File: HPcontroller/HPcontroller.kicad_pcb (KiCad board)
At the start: 4 copper layers, 100 x 39.8 mm, 64 parts, among them J1 Conn_01x02_Pin, J2 UJ20-C-H-G-SMT-1-P16-TR, J5 54-00174, SW1 SW_SPST, U1 PSSI2021SAY, U2 MCP3021A1T-E/OT, U4 NCP81071B, U5 AP33771C, U6 LM2904, U7 Adafruit_QTPY_ESP32-C3

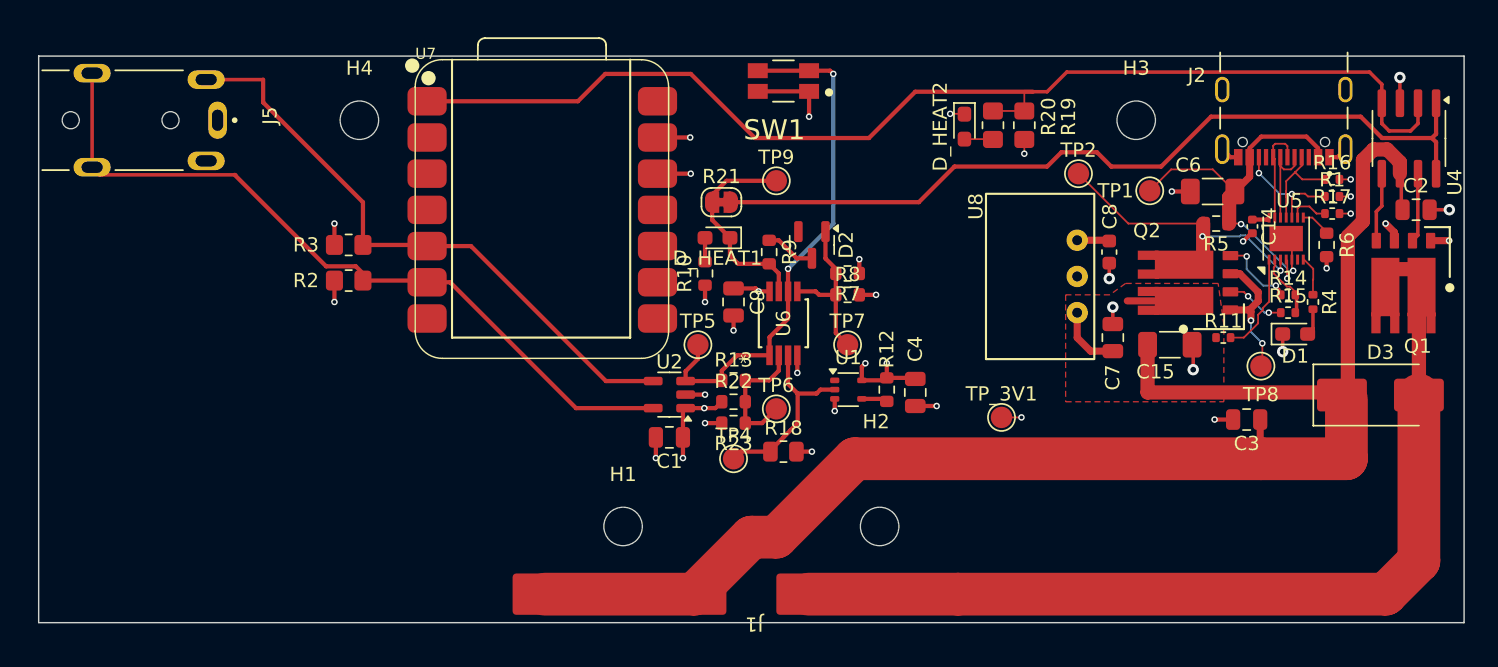
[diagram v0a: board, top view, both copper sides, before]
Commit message: released rev c - op amp swap not fixed!
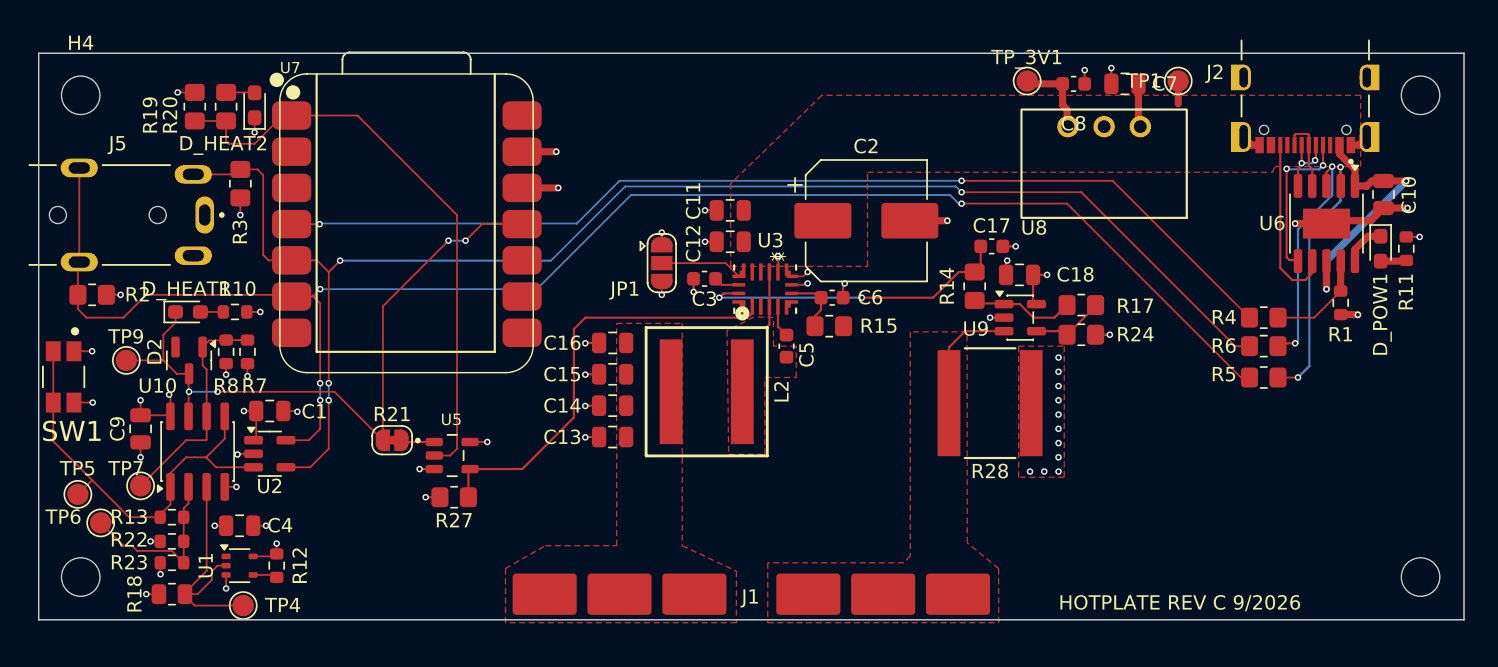
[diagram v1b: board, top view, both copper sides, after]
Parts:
- removed D1: LED, LED_SMD:LED_0603_1608Metric_Pad1.05x0.95mm_HandSolder
- removed D3: D, Diode_SMD:D_SMB_Handsoldering
- removed Q1, Q2: ~, hotplate_Library:LFPAK56D
- removed R16: 5k1 1%, Resistor_SMD:R_0402_1005Metric
- removed R9: 0, Resistor_SMD:R_0603_1608Metric
- removed TP2, TP8: TestPoint, TestPoint:TestPoint_Pad_D1.5mm
- removed U4: NCP81071B, Package_SO:SOIC-8_3.9x4.9mm_P1.27mm
- added C10: 10uF, Capacitor_SMD:C_0805_2012Metric, F.Cu at (179.6, 128.0)
- added C11: 10uF, Capacitor_SMD:C_0805_2012Metric, F.Cu at (133.8, 129.1)
- added C12: 10uF, Capacitor_SMD:C_0805_2012Metric, F.Cu at (133.8, 131.3)
- added C13: 10uF, Capacitor_SMD:C_0805_2012Metric, F.Cu at (125.5, 145.0)
- added C16: 10uF, Capacitor_SMD:C_0805_2012Metric, F.Cu at (125.5, 138.4)
- added C17: C, Capacitor_SMD:C_0603_1608Metric, F.Cu at (152.1, 131.6)
- added C18: 1uF, Capacitor_SMD:C_0805_2012Metric, F.Cu at (154.1, 133.6)
- added C5: 220n, Capacitor_SMD:C_0603_1608Metric, F.Cu at (137.7, 138.6)
- added D_POW1: LED, LED_SMD:LED_0603_1608Metric_Pad1.05x0.95mm_HandSolder, F.Cu at (179.4, 131.8)
- added JP1: Jumper_3_Open, Jumper:SolderJumper-3_P1.3mm_Open_RoundedPad1.0x1.5mm, F.Cu at (129.0, 132.8)
- added L2: 22u, HPcontroller_kimera:WE-XHMI_8080, F.Cu at (132.1, 141.8)
- added R24: 1.37k, Resistor_SMD:R_0805_2012Metric_Pad1.20x1.40mm_HandSolder, F.Cu at (158.4, 137.8)
- added R27: 10k, Resistor_SMD:R_0805_2012Metric_Pad1.20x1.40mm_HandSolder, F.Cu at (114.4, 149.2)
- added R28: 30m, HPcontroller_kimera:STA_CSSH2728_STP, F.Cu at (152.0, 142.6)
- added U10: MCP6002-xMS, Package_SO:SOIC-8_3.9x4.9mm_P1.27mm, F.Cu at (96.4, 146.0)
- added U3: MP4423CGLE-P, HPcontroller_kimera:QFN-16_MPQ4423C_MNP, F.Cu at (136.2, 134.6)
- added U9: MCP6001-OT, Package_TO_SOT_SMD:SOT-23-5, F.Cu at (154.1, 136.6)
- C14: value 1uF 25V -> 10uF; footprint Capacitor_SMD:C_0402_1005Metric -> Capacitor_SMD:C_0805_2012Metric
- C15: value 10uF 50V -> 10uF; footprint Capacitor_SMD:C_1206_3216Metric_Pad1.33x1.80mm_HandSolder -> Capacitor_SMD:C_0805_2012Metric
- C2: value 1uF -> 100u; footprint Capacitor_SMD:C_0805_2012Metric -> Capacitor_SMD:CP_Elec_8x6.7
- C3: value 10u -> 1u; footprint Capacitor_SMD:C_0805_2012Metric -> Capacitor_SMD:C_0603_1608Metric
- C6: value 10uF 50V -> 220n; footprint Capacitor_SMD:C_1206_3216Metric_Pad1.33x1.80mm_HandSolder -> Capacitor_SMD:C_0603_1608Metric
- R1: value 5k1 1% -> 210k; footprint Resistor_SMD:R_0402_1005Metric -> Resistor_SMD:R_0603_1608Metric
- R11: footprint Resistor_SMD:R_0402_1005Metric -> Resistor_SMD:R_0603_1608Metric
- R14: value 10 -> 0; footprint Resistor_SMD:R_0402_1005Metric -> Resistor_SMD:R_0805_2012Metric_Pad1.20x1.40mm_HandSolder
- R15: footprint Resistor_SMD:R_0402_1005Metric -> Resistor_SMD:R_0805_2012Metric_Pad1.20x1.40mm_HandSolder
- R17: value 5k1 1% -> 5.9k; footprint Resistor_SMD:R_0402_1005Metric -> Resistor_SMD:R_0805_2012Metric_Pad1.20x1.40mm_HandSolder
- R4: value 1k -> 0; footprint Resistor_SMD:R_0402_1005Metric -> Resistor_SMD:R_0805_2012Metric_Pad1.20x1.40mm_HandSolder
- R5: value 5m -> 0; footprint Resistor_SMD:R_0603_1608Metric -> Resistor_SMD:R_0805_2012Metric_Pad1.20x1.40mm_HandSolder
- R6: value 26k -> 0; footprint Resistor_SMD:R_0603_1608Metric -> Resistor_SMD:R_0805_2012Metric_Pad1.20x1.40mm_HandSolder
- U5: value AP33771C -> SN74LVC1G08DBVR; footprint Package_DFN_QFN:DFN-14-1EP_3x3mm_P0.4mm_EP1.78x2.35mm -> HPcontroller_kimera:SOT95P280X145-5N
- U6: value LM2904 -> ~; footprint hotplate_Library:MINISO8_3P1X3P2X0P65_STM -> Package_SO:SSOP-10-1EP_3.9x4.9mm_P1mm_EP2.1x3.3mm
- moved U5 60.5 mm to (114.3, 146.3), turned to 0 degrees
- moved R19 58.2 mm to (96.2, 121.8), turned to 90 degrees
- moved H2 56.2 mm to (88.2, 154.8)
- moved H1 56.1 mm to (182.2, 154.8)
- moved SW1 54.6 mm to (87.0, 140.8), turned to -90 degrees
- moved R20 53.8 mm to (98.4, 121.8), turned to 90 degrees
- moved TP7 50.6 mm to (92.4, 148.4)
- moved D_HEAT2 49.8 mm to (100.4, 121.7), turned to 90 degrees
- moved C4 48.3 mm to (99.3, 151.2), turned to 180 degrees
- moved TP6 48.1 mm to (89.6, 151.0)
- moved TP9 47.3 mm to (91.4, 139.6)
- moved C14 46.6 mm to (125.5, 142.8), turned to 180 degrees
- moved TP5 44.7 mm to (88.0, 149.0)
- moved R12 44.5 mm to (102.0, 154.0)
- moved U1 44.5 mm to (99.3, 154.0)
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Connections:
- C14 pad 1: Net-(U5-V5V) -> Net-(J1-Pin_1)
- C15 pad 1: +28V -> Net-(J1-Pin_1)
- C3 pad 1: +28V -> Net-(U3-VCC)
- C6 pad 1: /USB POWER IN/VUSB_RAW -> GND
- C6 pad 2: GND -> Net-(U3-OUT)
- D2 pad 3: Net-(D2-K) -> /HEATER DRIVE/ENABLE_HEATER_DRIVE
- J1 pad 1: +28V -> Net-(J1-Pin_1)
- J2 pad A4_B9: /USB POWER IN/VUSB_RAW -> +28V
- J2 pad B4_A9: /USB POWER IN/VUSB_RAW -> +28V
- R1 pad 1: /USB POWER IN/CC2 -> GND
- R1 pad 2: GND -> Net-(U6-CFG1)
- R11 pad 1: +28V -> +3V3
- R11 pad 2: Net-(U5-Vout) -> Net-(D_POW1-A)
- R13 pad 2: Net-(U6A--) -> Net-(U10A--)
- R14 pad 1: Net-(Q2-G2) -> /HEATER DRIVE/FB
- R14 pad 2: Net-(U5-PWR_EN) -> Net-(R14-Pad2)
- R15 pad 1: Net-(Q2-G1) -> Net-(U3-OUT)
- R15 pad 2: Net-(U5-PWR_EN) -> Net-(J1-Pin_1)
- R17 pad 1: Net-(U5-ISel) -> Net-(R14-Pad2)
- R17 pad 2: GND -> Net-(U9--)
- R18 pad 1: Net-(U6A-+) -> Net-(U10A-+)
- R21 pad 2: Net-(U4-ENA) -> Net-(U5-A)
- R22 pad 2: Net-(U6A--) -> Net-(U10A--)
- R23 pad 1: Net-(U6A--) -> Net-(U10A--)
- R4 pad 1: Net-(U5-LED) -> Net-(U6-CFG1)
- R4 pad 2: Net-(D1-A) -> /USB POWER IN/CFG1
- R5 pad 1: /USB POWER IN/VUSB_RAW -> /USB POWER IN/CFG2/SCL
- R5 pad 2: Net-(Q2-D2) -> /SCL
- R6 pad 1: Net-(U5-VSel) -> /USB POWER IN/CFG3/SDA
- R6 pad 2: GND -> /SDA
- TP1 pad 1: /USB POWER IN/VUSB_RAW -> +28V
- TP4 pad 1: Net-(U6A-+) -> Net-(U10A-+)
- TP6 pad 1: Net-(U6A--) -> Net-(U10A--)
- U1 pad 2: Net-(U6A-+) -> Net-(U10A-+)
- U5 pad 1: Net-(U5-Vout) -> Net-(U5-A)
- U5 pad 2: Net-(U5-PWR_EN) -> /HEAT_DRIVE
- U5 pad 3: Net-(Q2-D2) -> GND
- U5 pad 4: /USB POWER IN/VUSB_RAW -> /HEATER DRIVE/EN
- U5 pad 5: GND -> +3V3
- U6 pad 1: Net-(SW1-B) -> +28V
- U6 pad 2: Net-(U6A--) -> /USB POWER IN/CFG2/SCL
- U6 pad 3: Net-(U6A-+) -> /USB POWER IN/CFG3/SDA
- U6 pad 4: GND -> /USB POWER IN/DP
- U6 pad 5: Net-(D2-A) -> /USB POWER IN/DN
- U6 pad 6: Net-(SW1-B) -> /USB POWER IN/CC1
- U6 pad 7: /HEATER DRIVE/ENABLE_HEATER_DRIVE -> /USB POWER IN/CC2
- U6 pad 8: +3V3 -> +28V
- U7 pad 11: unconnected-(U7-MOSI-Pad11) -> /HEATER DRIVE/ENABLE_HEATER_DRIVE
- U7 pad 4: unconnected-(U7-A3-Pad4) -> /USB POWER IN/CFG1
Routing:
- net +28V: track 117.6 -> 23.4 mm, vias 0 -> 2
- net /USB POWER IN/CFG1: track 0.00 -> 72.4 mm, vias 0 -> 2
- net /SDA: track 42.8 -> 103.6 mm, vias 0 -> 4
- net /SCL: track 53.3 -> 113.6 mm, vias 0 -> 4
- net Net-(J1-Pin_2): track 66.9 -> 8.25 mm
- net Net-(U4-ENA): track 58.3 -> 0.00 mm
- net /HEAT_DRIVE: track 83.2 -> 41.8 mm
- net /HEATER DRIVE/ENABLE_HEATER_DRIVE: track 14.9 -> 48.1 mm, vias 0 -> 4
- net /HEATER DRIVE/EN: track 0.00 -> 30.5 mm
- net /USB POWER IN/VUSB_RAW: track 26.7 -> 0.00 mm, vias 2 -> 0
- net /HEATER DRIVE/FB: track 0.00 -> 22.3 mm, vias 0 -> 2
- net Net-(Q2-D2): track 20.4 -> 0.00 mm, vias 2 -> 0
- net /USB POWER IN/CFG2/SCL: track 0.00 -> 18.7 mm, vias 0 -> 2
- net Net-(U10A-+): track 0.00 -> 16.7 mm
- net /USB POWER IN/CFG3/SDA: track 0.00 -> 16.4 mm, vias 0 -> 2
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- added copper zone on In2.Cu, net +3V3
- added copper zone on F.Cu, net GND
- added copper zone on In1.Cu, net GND
- added copper zone on F.Cu, net Net-(C5-Pad2)
- added copper zone on F.Cu, net Net-(J1-Pin_1)
- added copper zone on F.Cu, net Net-(J1-Pin_2)
- removed copper zone on In1.Cu, net +3V3
- removed copper zone on In2.Cu, net GND
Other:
- board text added: "HOTPLATE REV C 9/2026"

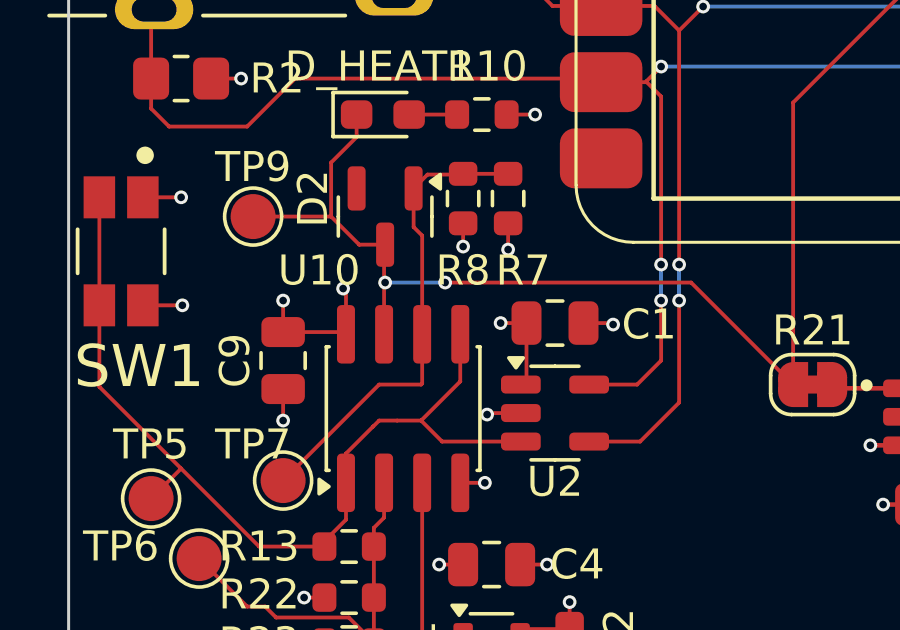
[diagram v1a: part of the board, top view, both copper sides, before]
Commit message: fixed op amp input swap on latch
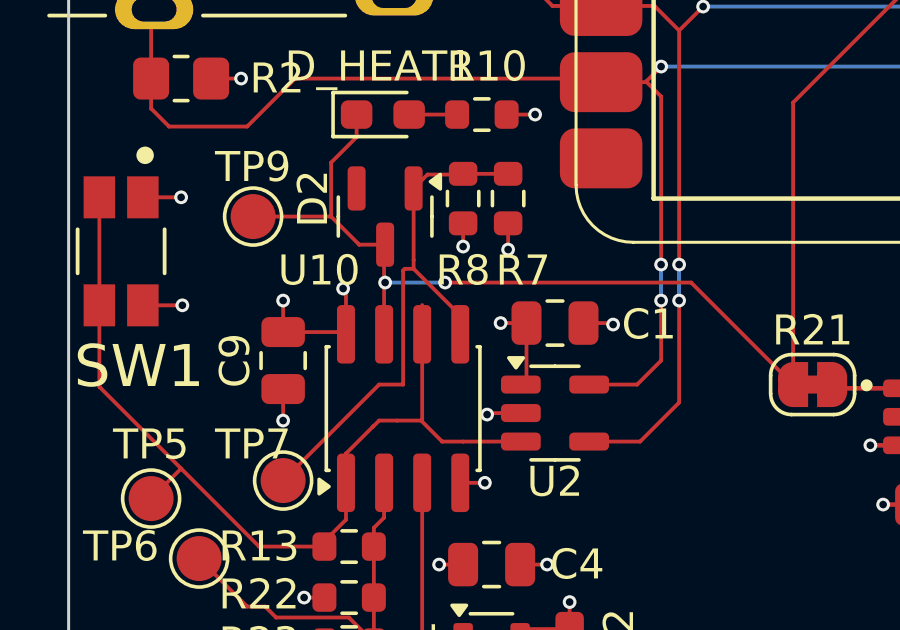
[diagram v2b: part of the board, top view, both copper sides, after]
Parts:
- C1, C18, C4, C9: value 1uF -> 1UF
- C10, C11, C12, C13, C14, C15, C16, C7: value 10uF -> 10UF
- C2: value 100u -> 82UF
- C3: value 1u -> 1UF
- C5, C6: value 220n -> 220NF
- C8: value 22uF -> 22UF
- L2: value 22u -> 22UH
- R1: value 210k -> 210K
- R13: value 1210 -> 1.21K
- R17: value 5.9k -> 5.9K
- R19, R27: value 10k -> 10K
- R2, R3: value 4k7 -> 4.7K
- R22: value 1300 -> 1.3K
- R23: value 1020 -> 1.02K
- R24: value 1.37k -> 1.37K
- R28: value 30m -> 0.03
- R8: value 1200 -> 1.2K
- U6: value ~ -> CH244A
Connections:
- U10 pad 5: Net-(SW1-B) -> Net-(D2-A)
- U10 pad 6: Net-(D2-A) -> Net-(SW1-B)
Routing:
- net Net-(D2-A): track 15.9 -> 18.4 mm
